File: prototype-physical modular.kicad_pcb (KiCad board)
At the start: 2 copper layers, 100 x 164 mm, 171 parts, among them CON1 BARREL_JACK, CON2 SD_Card, IC1 ATMEGA2560-A, J1 MIDI_IN, J2 MIDI_OUT, P1 POWER, P15 PH, P16 PF, P17 SD_PINS, P18 3VI2C, P2 FTDI, P3 SPI, P4 BUSTI, P5 BUSTO, P7 PA, Q1 BSS138, Q2 BSS138, Q3 BSS138, Q4 BSS138, Q5 BSS138, Q6 BSS138, SW1 SW_PUSH, SW10 SW_PUSH, SW11 SW_PUSH, SW12 SW_PUSH, SW13 SW_PUSH, SW14 SW_PUSH, SW2 ROTARY_ENCODER_SWITCH, SW3 SW_PUSH, SW4 SW_PUSH, SW5 SW_PUSH, SW6 SW_PUSH, SW7 SW_PUSH, SW8 SW_PUSH, SW9 SW_PUSH, U1 NCP1117ST50T3G, U2 6N138, Y1 16MHz

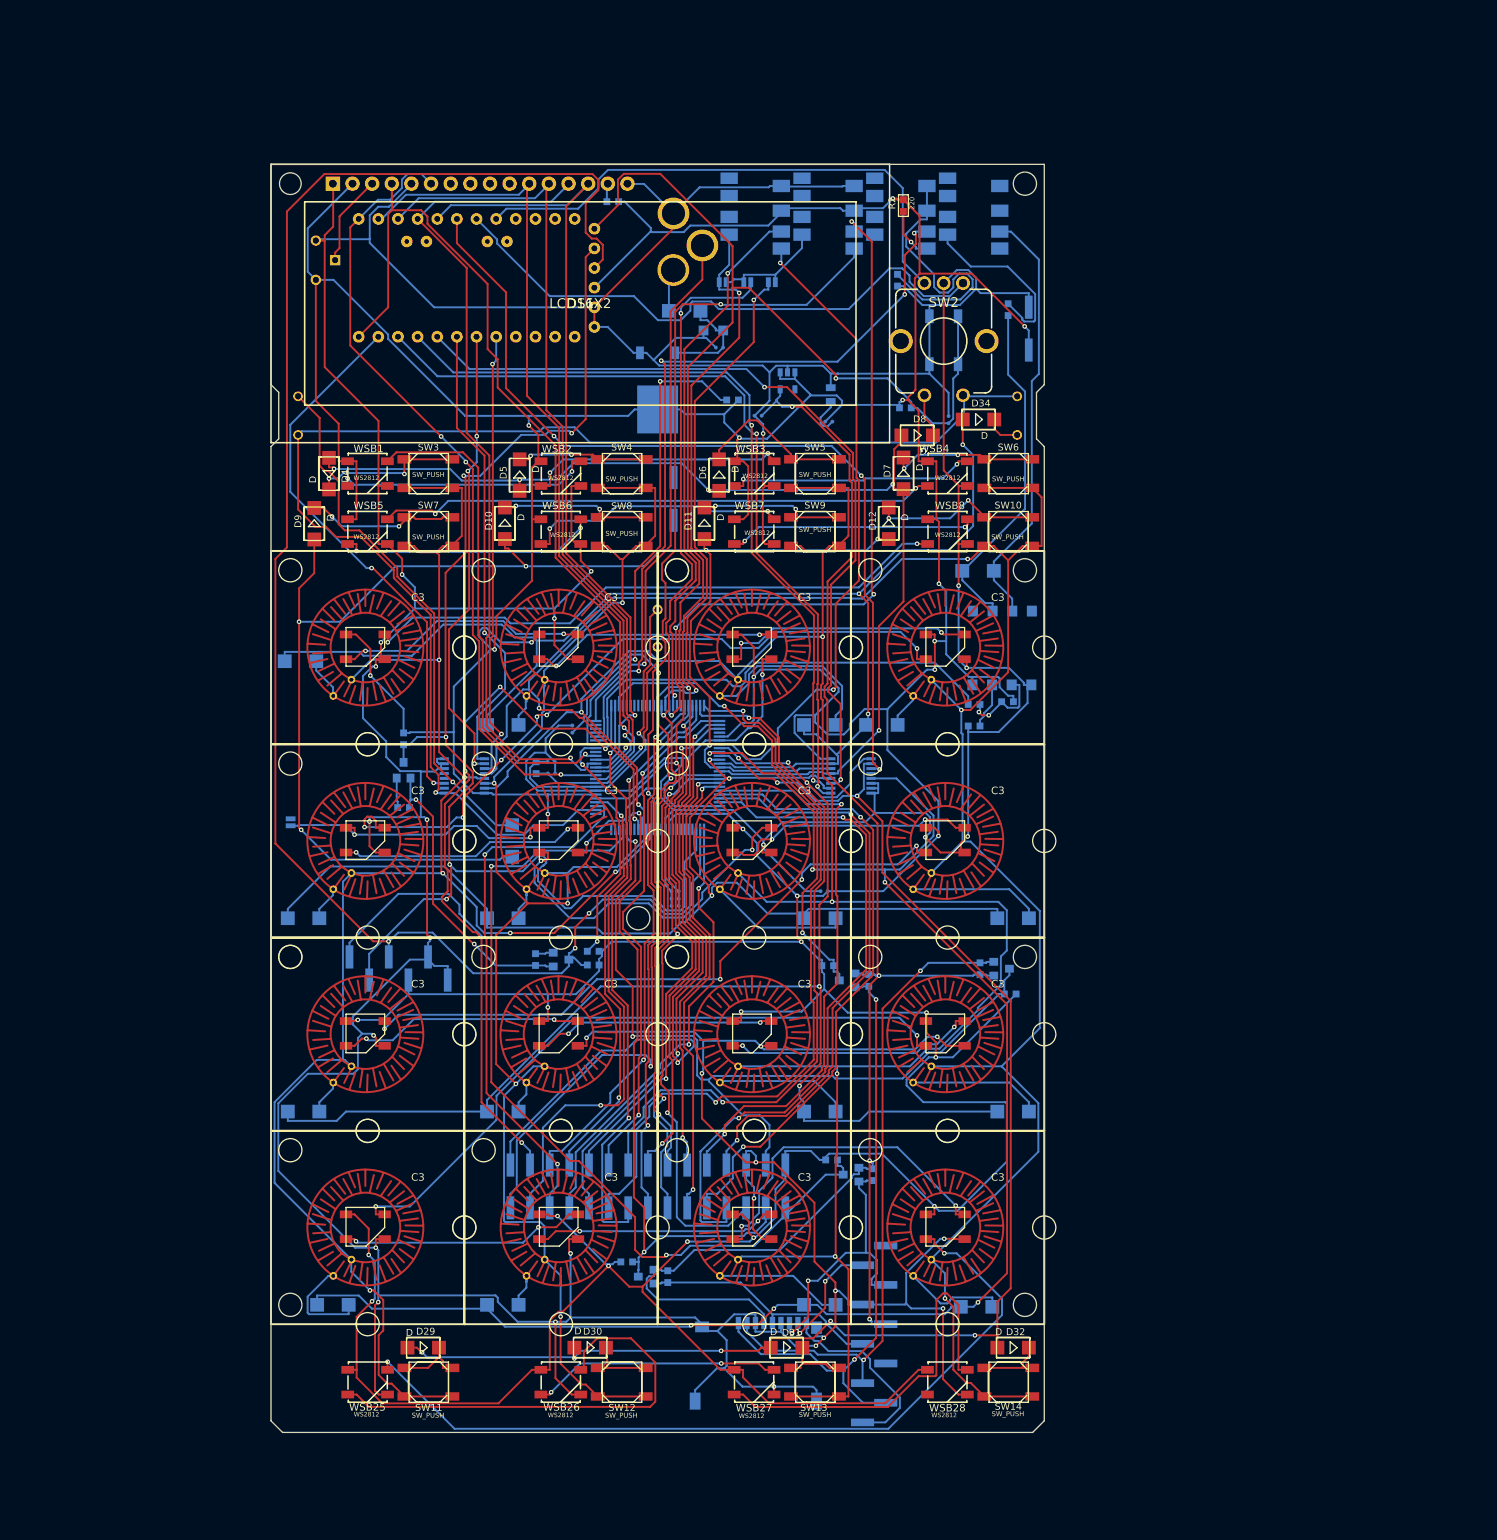
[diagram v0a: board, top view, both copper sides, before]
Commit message: Add I2C enabling Jumpers testing and beefing up TBN communication different arrangement try in PCB
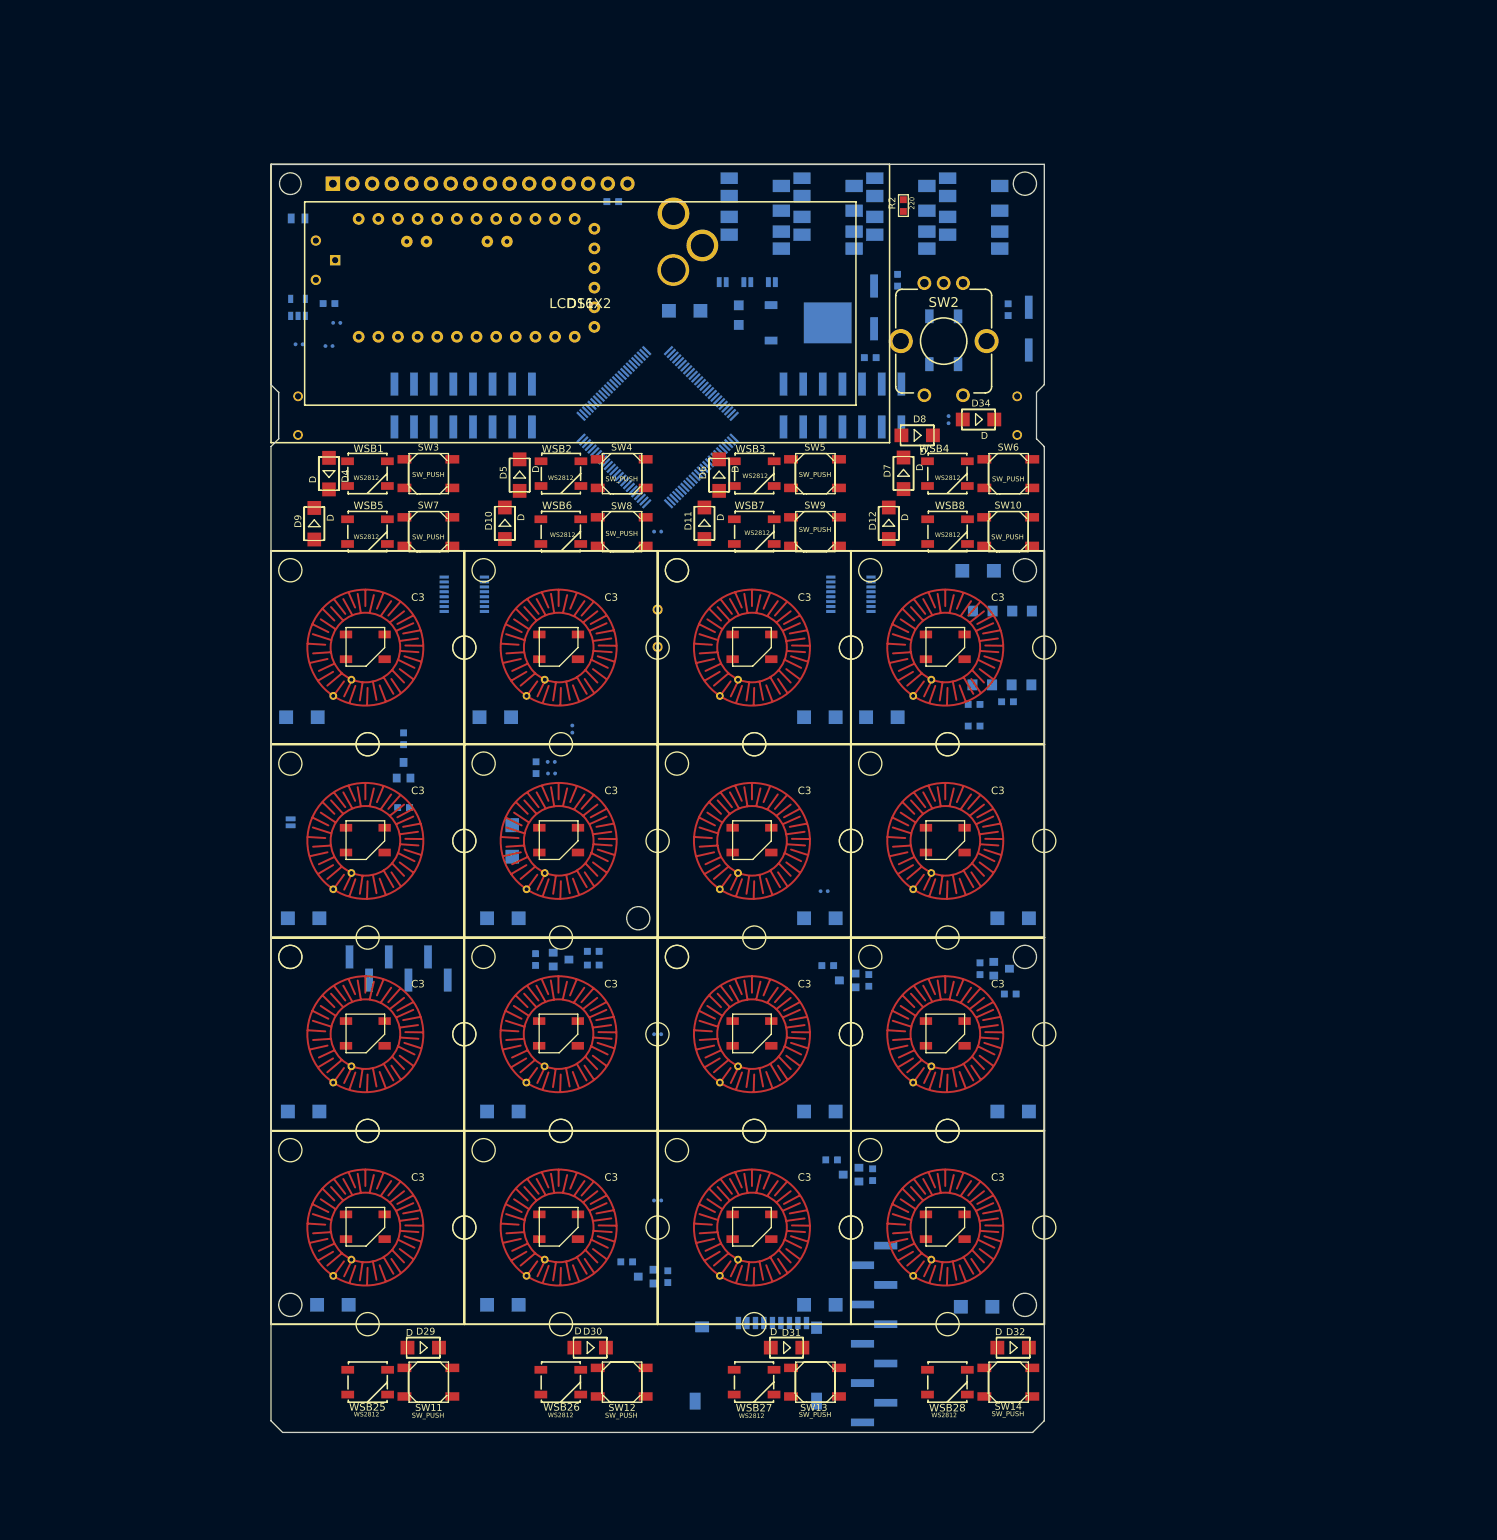
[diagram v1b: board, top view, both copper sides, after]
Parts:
- moved P15 102.1 mm to (19.8, 31.2)
- moved P16 102.1 mm to (70.1, 31.2)
- moved P3 102.1 mm to (79.0, 31.2)
- moved P7 102.1 mm to (29.9, 31.2)
- moved D2 72.6 mm to (3.50, 7.00), turned to 0 degrees
- moved R1 69.2 mm to (3.64, 23.3)
- moved 3v3regu1 64.0 mm to (3.50, 18.5), turned to 90 degrees
- moved C3 55.8 mm to (8.50, 20.5)
- moved R10 53.7 mm to (7.50, 18.0), turned to 270 degrees
- moved C1 50.5 mm to (7.50, 23.5)
- moved C4 46.6 mm to (50.0, 47.5)
- moved IC1 44.0 mm to (50.0, 34.0), turned to 135 degrees
- moved C5 39.1 mm to (50.0, 134.0)
- moved P18 35.9 mm to (78.0, 18.5), turned to 90 degrees
- moved MUXA1 23.5 mm to (25.0, 55.6)
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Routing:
- net GND: track 1036.4 -> 0.00 mm, vias 33 -> 0
- net +5V: track 988.6 -> 0.00 mm, vias 31 -> 0
- net /MUXAX2: track 292.9 -> 0.00 mm, vias 6 -> 0
- net /MUXAX3: track 287.0 -> 0.00 mm, vias 5 -> 0
- net /RESET: track 283.5 -> 0.00 mm, vias 4 -> 0
- net /RX0: track 223.2 -> 0.00 mm, vias 3 -> 0
- net /MUXAX0: track 220.8 -> 0.00 mm, vias 6 -> 0
- net +3V3: track 211.0 -> 0.00 mm, vias 4 -> 0
- net /MUXBX5: track 211.0 -> 0.00 mm, vias 6 -> 0
- net /MUXBX1: track 201.5 -> 0.00 mm, vias 6 -> 0
- net /MUXAX1: track 190.4 -> 0.00 mm, vias 5 -> 0
- net /MUXBX6: track 188.4 -> 0.00 mm, vias 8 -> 0
- net /MUXAX4: track 179.1 -> 0.00 mm, vias 1 -> 0
- net /MUXBX4: track 175.2 -> 0.00 mm, vias 4 -> 0
- net /TX0: track 175.1 -> 0.00 mm, vias 5 -> 0
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
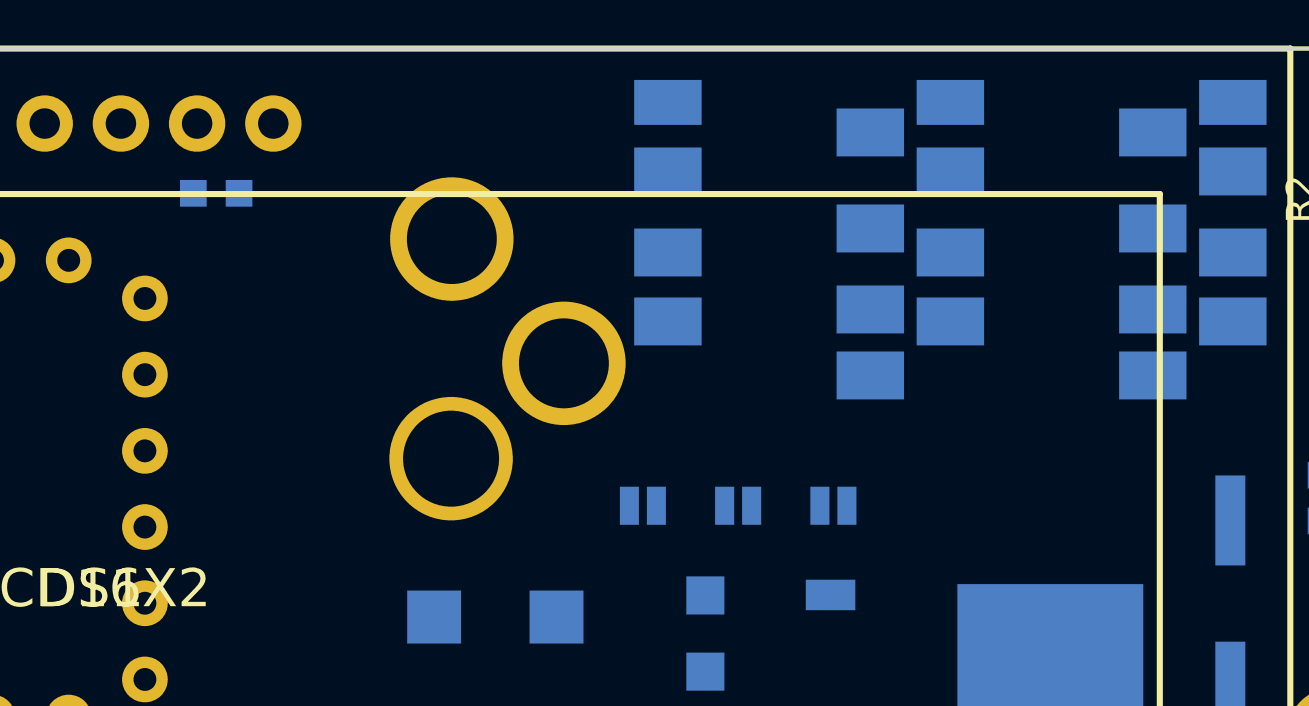
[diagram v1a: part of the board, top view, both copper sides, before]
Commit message: - testing communications with all the rest of the hardware - spotted wrongly connected CS pin for SD card
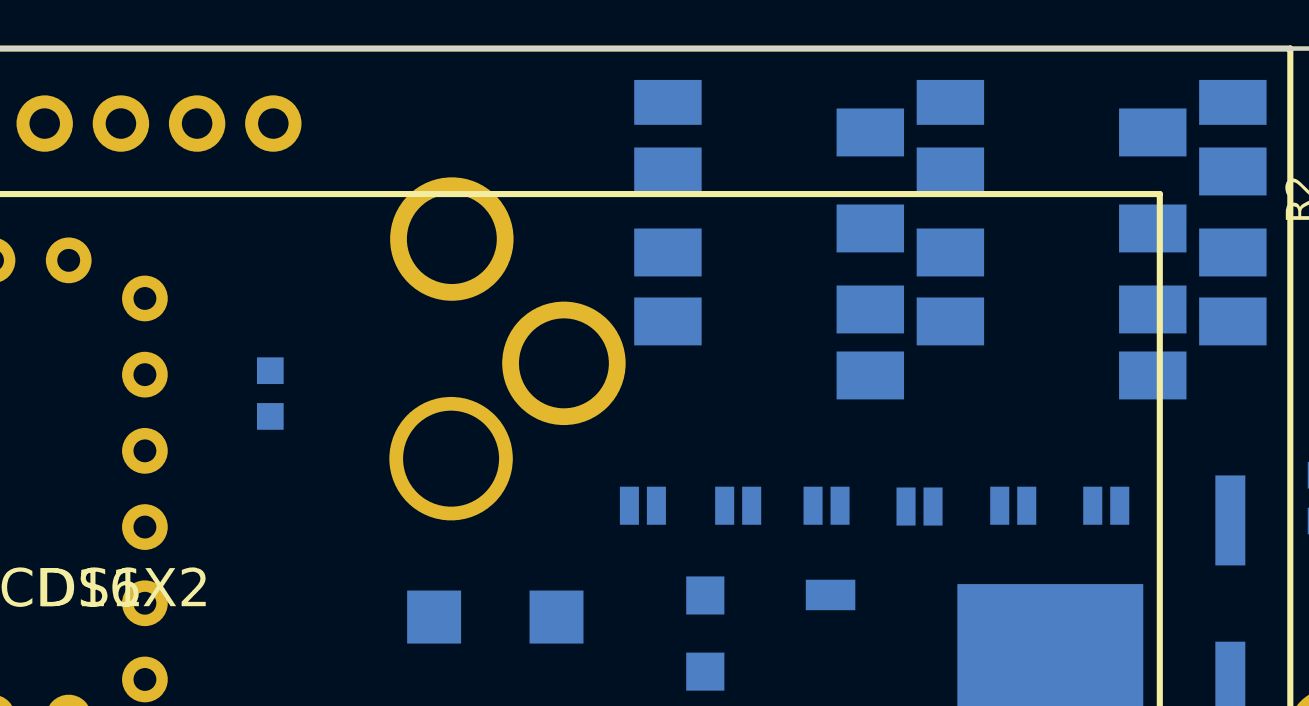
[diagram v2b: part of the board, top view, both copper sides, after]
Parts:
- added JP3: JkI2C0, SparkFun-Passives:PAD-JUMPER-2-NO_YES_SILK, B.Cu at (73.9, 15.2)
- added JP4: JkI2C0, SparkFun-Passives:PAD-JUMPER-2-NO_YES_SILK, B.Cu at (67.6, 15.3)
- added JP5: JkI2C0, SparkFun-Passives:PAD-JUMPER-2-NO_YES_SILK, B.Cu at (70.8, 15.2)
- moved R23 6.91 mm to (46.0, 11.5), turned to 0 degrees
- moved PJ2COM1 0.23 mm to (64.5, 15.2)
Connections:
- IC1 pad 19: Net-(IC1-Pad19) -> /5VSD_CS
- IC1 pad 53: /5VSD_CS -> Net-(IC1-Pad53)
